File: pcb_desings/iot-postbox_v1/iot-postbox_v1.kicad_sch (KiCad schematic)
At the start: 2 parts

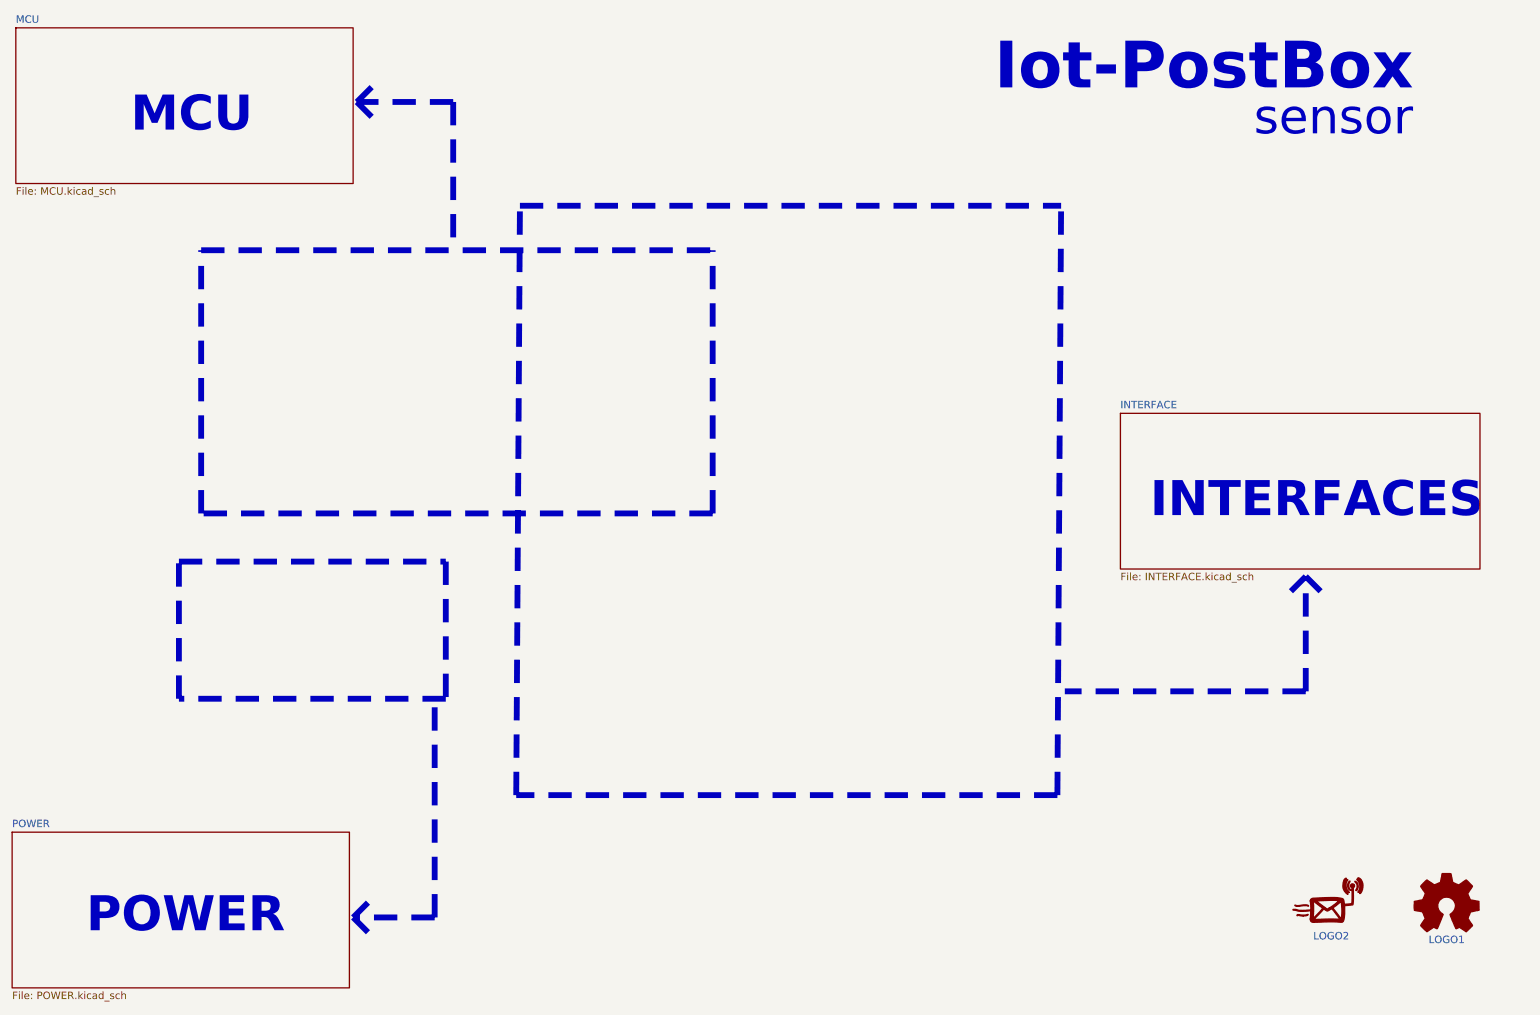
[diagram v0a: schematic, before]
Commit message: Added iot-postbox_v1 sch to v1.1. Added minor documentation
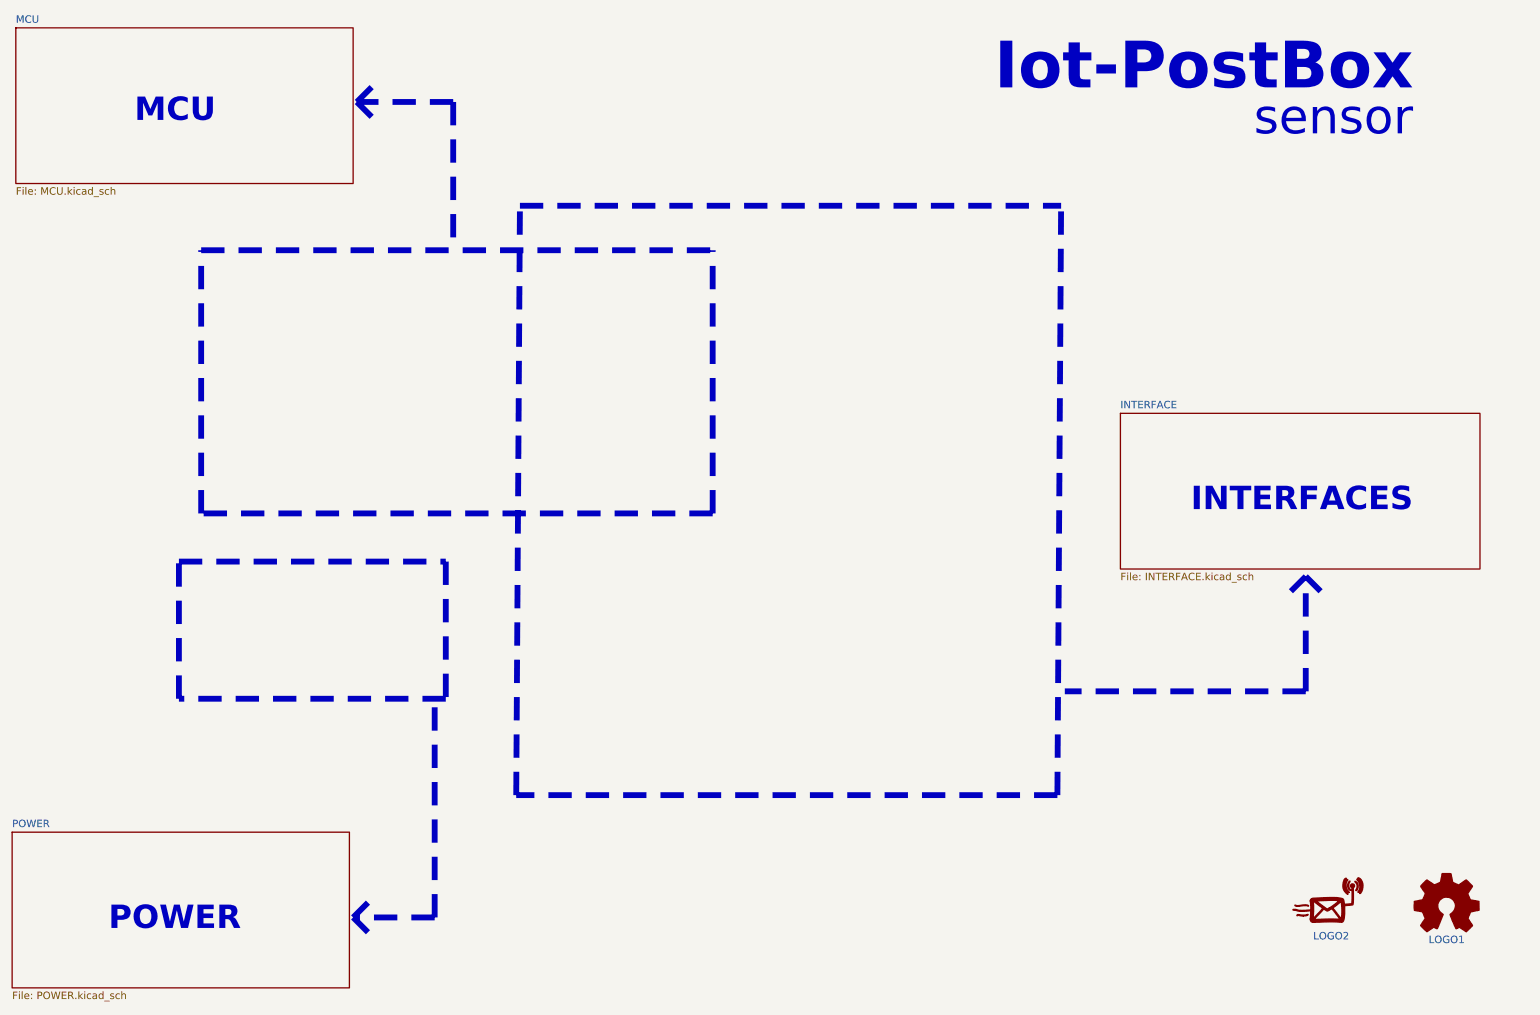
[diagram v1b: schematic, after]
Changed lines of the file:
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@@
     (title "IoT-PostBox")
     (date "28.05.2022")
-    (rev "v1.0")
+    (rev "v1.1")
     (comment 1 "https://github.com/paclema/iot-postbox")
     (comment 2 "IoT-PostBox board based on ESP32-S2")
@@
     (effects (font (size 8 8) (thickness 0.7976) bold) (justify left bottom))
   )
-  (text "POWER" (at 37.465 177.8 0)
-    (effects (font (size 6 6) (thickness 0.5994) bold) (justify left bottom))
+  (text "POWER" (at 41.275 177.165 0)
+    (effects (font (size 4 4) (thickness 0.5994) bold) (justify left bottom))
   )
-  (text "INTERFACES" (at 219.71 106.68 0)
-    (effects (font (size 6 6) (thickness 0.5994) bold) (justify left bottom))
+  (text "INTERFACES" (at 226.695 105.41 0)
+    (effects (font (size 4 4) (thickness 0.5994) bold) (justify left bottom))
   )
-  (text "MCU" (at 45.085 40.64 0)
-    (effects (font (size 6 6) (thickness 0.5994) bold) (justify left bottom))
+  (text "MCU" (at 45.72 38.735 0)
+    (effects (font (size 4 4) (thickness 0.5994) bold) (justify left bottom))
   )
   (text "sensor" (at 237.49 41.275 0)

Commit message: Created iot-postbox v1.2 migrating to kicad v9. Fixed missing 3d designs, replaced horizontal footprints for some connectors.
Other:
- company: (none) -> @paclema
